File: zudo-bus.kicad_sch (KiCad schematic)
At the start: 21 parts, among them P1 WJ500V-5.08-2P-14-00A, P2 WJ500V-5.08-2P-14-00A, P3 Faston -12V, P4 Faston GND, P5 Faston +12V, P6 Faston +5V, U1 AMS1117-5.0

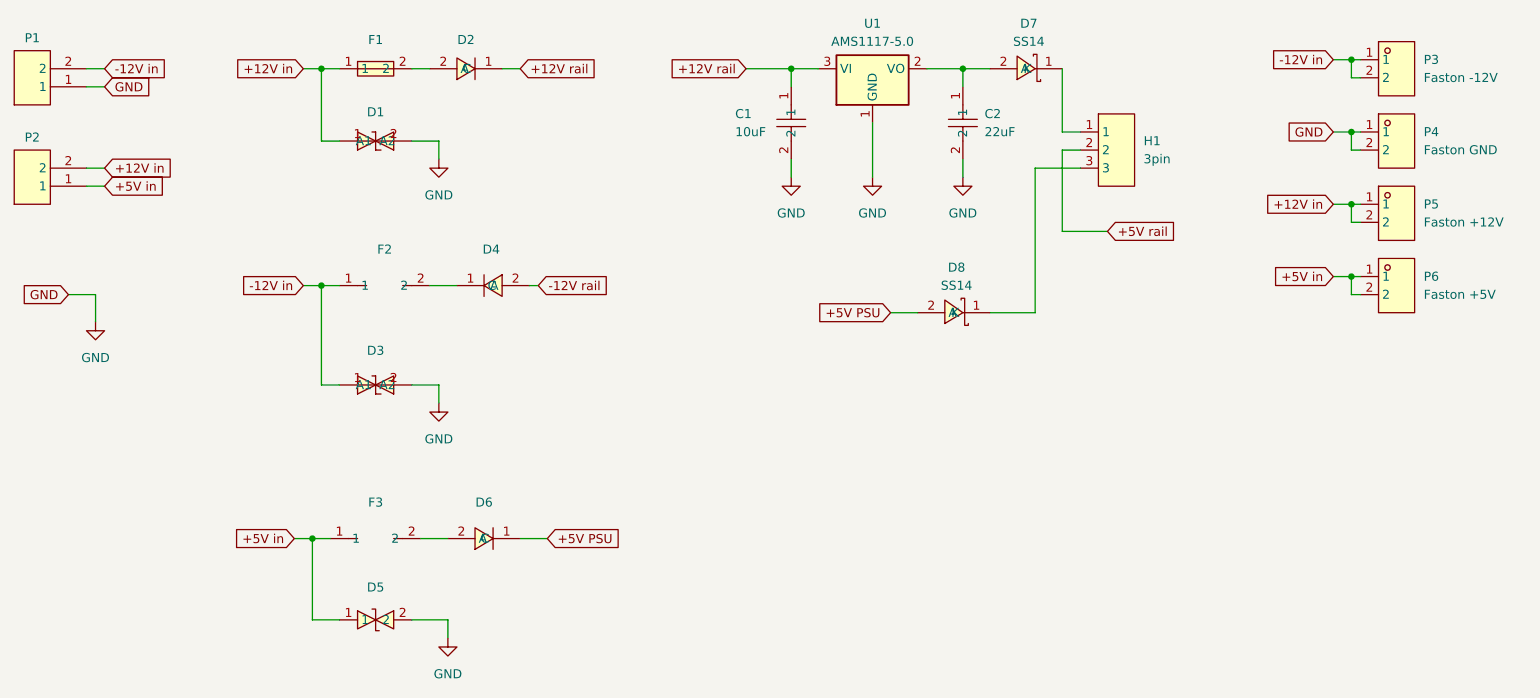
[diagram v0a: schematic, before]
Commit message: Add Diagram6 (FASTON chaining) and Diagram7 (IDC headers)
Schematic reorganization:
- Split into hierarchical sheets (in-out.kicad_sch, rail.kicad_sch)
- in-out: Input, protection, LDO, FASTON (Diagrams 1-6)
- rail: IDC headers and decoupling capacitors (Diagram7)

Diagram6 - FASTON chaining connectors:
- P3 (-12V), P4 (GND), P5 (+12V), P6 (+5V)
- Connected to input nets for daisy-chaining bus boards

Diagram7 - IDC headers with new numbering scheme:
- J101-J108: IDC headers (J1XX = unit number)
- C101-C108: -12V decoupling (C1XX matches header)
- C201-C208: +12V decoupling (C2XX matches header)
- Expandable numbering allows easy addition of more units

Documentation updates:
- Added schematic file structure section
- Updated component numbering throughout
- Fixed IDC header references (J1-J8 -> J101-J108)

Co-Authored-By: Claude <noreply@anthropic.com>
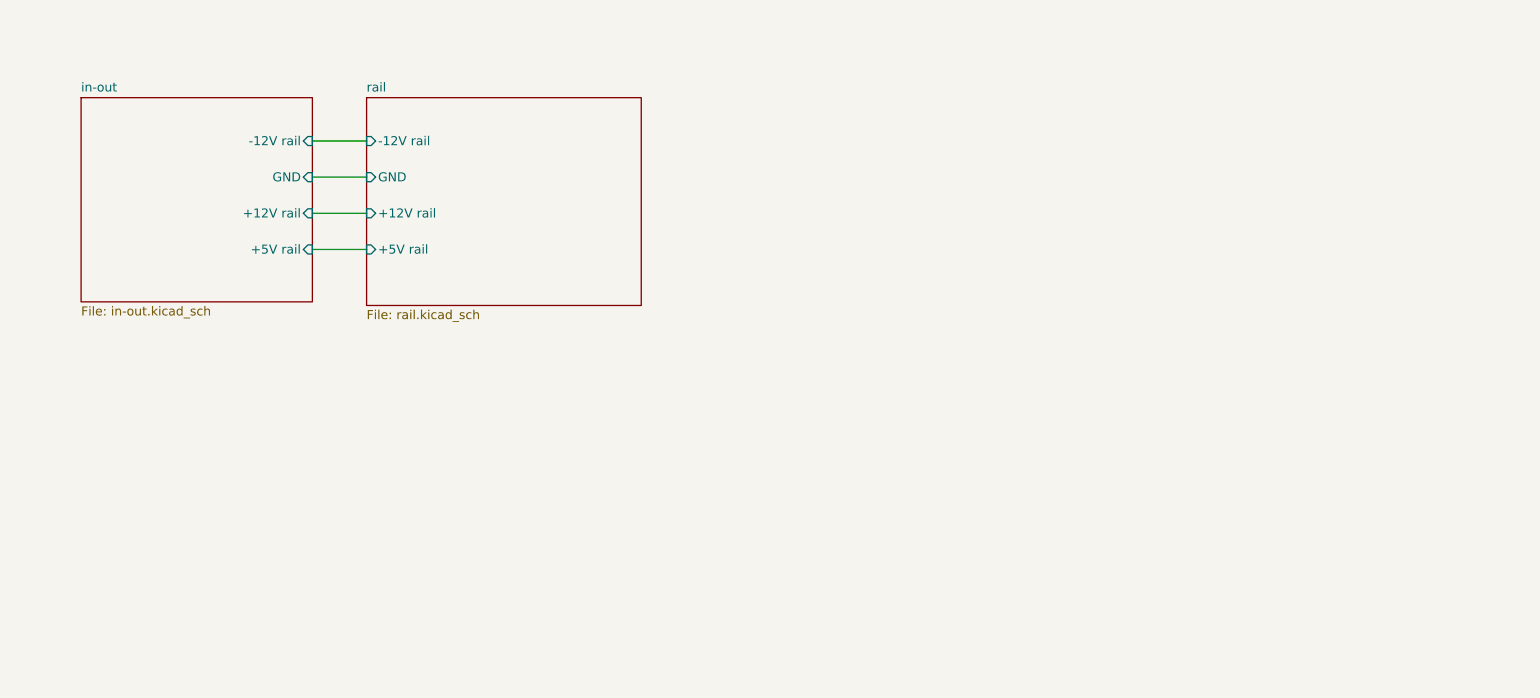
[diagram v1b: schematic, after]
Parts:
- removed C1: 10uF, samsung-caps:C0805, symbol samsung-caps:CL21A106KAYNNNE
- removed C2: 22uF, samsung-caps:C0805, symbol samsung-caps:CL21A226MAQNNNE
- removed D1, D3: SMF12CA_C353317, zudo-bus:SOD-123FL_L2.8-W1.8-LS3.7-BI, symbol zudo-bus-new-protection:SMF12CA_C353317
- removed D2, D4, D6: SM4007PL, easyeda2kicad:SOD-123F_L2.8-W1.8-LS3.7-RD, symbol zudo-bus:SM4007PL
- removed D5: SMF5.0CA_C908214, :SOD-123_L2.8-W1.8-LS3.7-BI, symbol zudo-bus-protection:SMF5.0CA_C908214
- removed D7, D8: SS14, zudo-bus:SMA_L4.2-W2.6-LS5.0-RD_1, symbol zudo-bus-new-protection:SS14
- removed F1: BSMD1812-200-30V, :F1812, symbol zudo-bus-protection:BSMD1812-200-30V
- removed F2, F3: BSMD1812-150-33V, :F1812, symbol zudo-bus-protection:BSMD1812-150-33V
- removed H1: 3pin, easyeda2kicad:HDR-TH_3P-P2.54-V-M-1, symbol zudo-bus:Header-Male-2.54_1x3
- removed P1, P2: WJ500V-5.08-2P-14-00A, easyeda2kicad:CONN-TH_2P-P5.00_WJ500V-5.08-2P, symbol zudo-bus:WJ500V-5.08-2P-14-00A
- removed P3: Faston -12V, easyeda2kicad:CONN-TH_1217754-1, symbol zudo-bus:1217754-1
- removed P4: Faston GND, easyeda2kicad:CONN-TH_1217754-1, symbol zudo-bus:1217754-1
- removed P5: Faston +12V, easyeda2kicad:CONN-TH_1217754-1, symbol zudo-bus:1217754-1
- removed P6: Faston +5V, easyeda2kicad:CONN-TH_1217754-1, symbol zudo-bus:1217754-1
- removed U1: AMS1117-5.0, Package_TO_SOT_SMD:SOT-223-3_TabPin2, symbol Regulator_Linear:AMS1117-5.0
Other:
- added sheet in-out (in-out.kicad_sch)
- added sheet rail (rail.kicad_sch)
